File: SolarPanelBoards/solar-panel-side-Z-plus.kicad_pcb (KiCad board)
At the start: 2 copper layers, 97 x 97.4 mm, 40 parts, among them J1 Conn_01x06, J3 Conn_01x02, Q12 BSS138DWQ-7, Q13 BSS138DWQ-7, Q7 MBT2222ADW1T1, Q8 MBT2222ADW1T1, U1 OPT3001DNPT

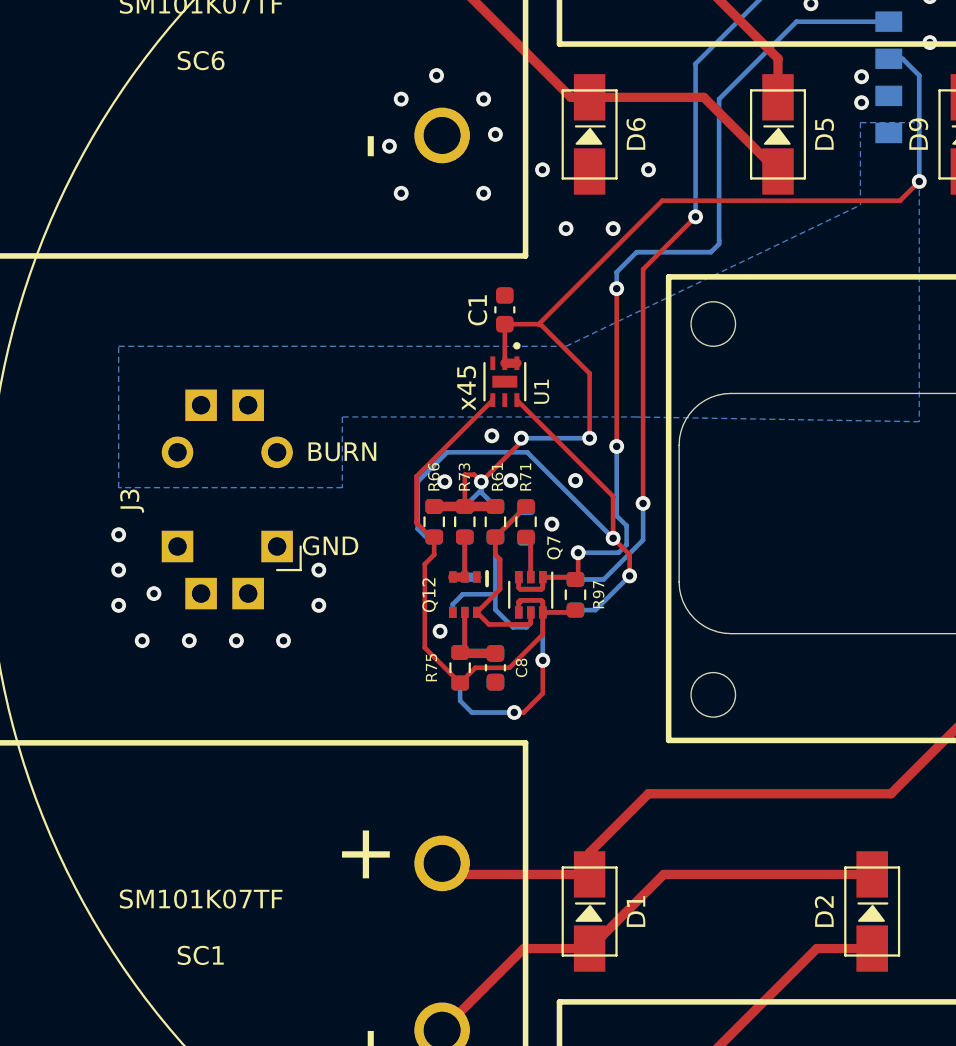
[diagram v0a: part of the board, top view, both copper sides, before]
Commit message: Updated libraries and batteryboard/solarpanelboards accordingly
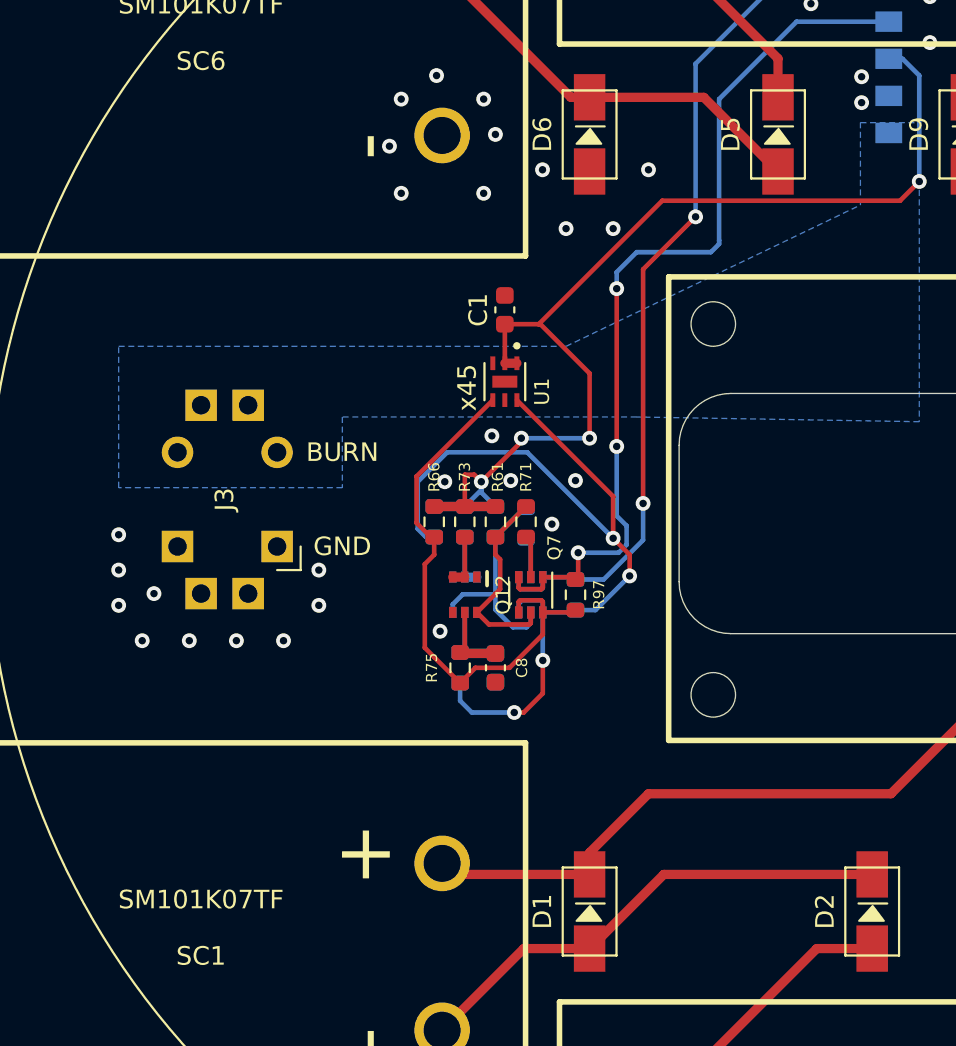
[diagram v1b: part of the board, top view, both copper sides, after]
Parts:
- D1, D2, D3, D4, D5, D6, D9: footprint sapling:DO-214AC -> sputnik2U:DO-214AC
- J3: footprint sapling:Burn_Wire_Connection -> sputnik2U:Burn_Wire_Connection
- Q12, Q13: footprint sapling:BSS138DWQ-7 -> sputnik2U:BSS138DWQ-7
- SC1, SC2, SC3, SC4, SC5, SC6: footprint sapling:SM101K07TF -> sputnik2U:SM101K07TF
- U1: footprint sapling:OPT3001 -> sputnik2U:OPT3001
- renumbered H3 to H1, H4 to H2, H5 to H3, H6 to H4
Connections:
- J1 pad S1: (no net) -> unconnected-(J1-PadS1)
- J1 pad S2: (no net) -> unconnected-(J1-PadS2)
- U1 pad 5: (no net) -> unconnected-(U1-Pad5)

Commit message: Updated schematics, added/refined libraries
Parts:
- D1, D2, D3, D4, D5, D6, D9: footprint sputnik2U:DO-214AC -> panels:DO-214AC
- J1: footprint sapling:MOLEX_2053380006 -> panels:MOLEX_2053380006
- J3: footprint sputnik2U:Burn_Wire_Connection -> panels:Burn_Wire_Connection
- Q12, Q13: footprint sputnik2U:BSS138DWQ-7 -> panels:BSS138DWQ-7
- SC1, SC2, SC3, SC4, SC5, SC6: footprint sputnik2U:SM101K07TF -> panels:SM101K07TF
- U1: footprint sputnik2U:OPT3001 -> panels:OPT3001
- renumbered H4 to H1, H1 to H3, H3 to H4
